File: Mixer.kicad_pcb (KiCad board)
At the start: 2 copper layers, 60 x 100 mm, 44 parts, among them J1 Audio-Jack-2_Switch, J2 Conn_02x05_Odd_Even, J3 Audio-Jack-2_Switch, J4 Audio-Jack-2_Switch, J5 Audio-Jack-2_Switch, J6 Audio-Jack-2_Switch, J7 Audio-Jack-2_Switch, U1 TL074

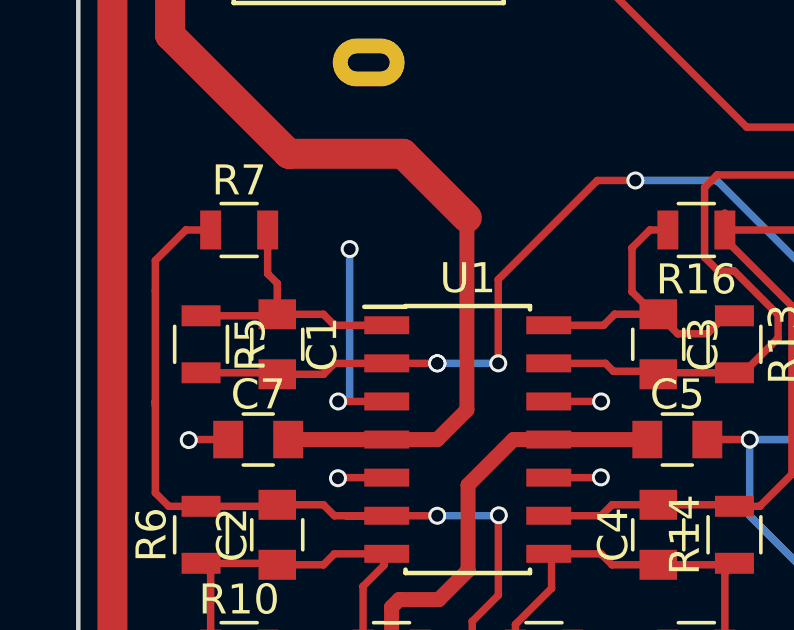
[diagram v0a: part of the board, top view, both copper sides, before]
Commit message: Fixed DRC violation.
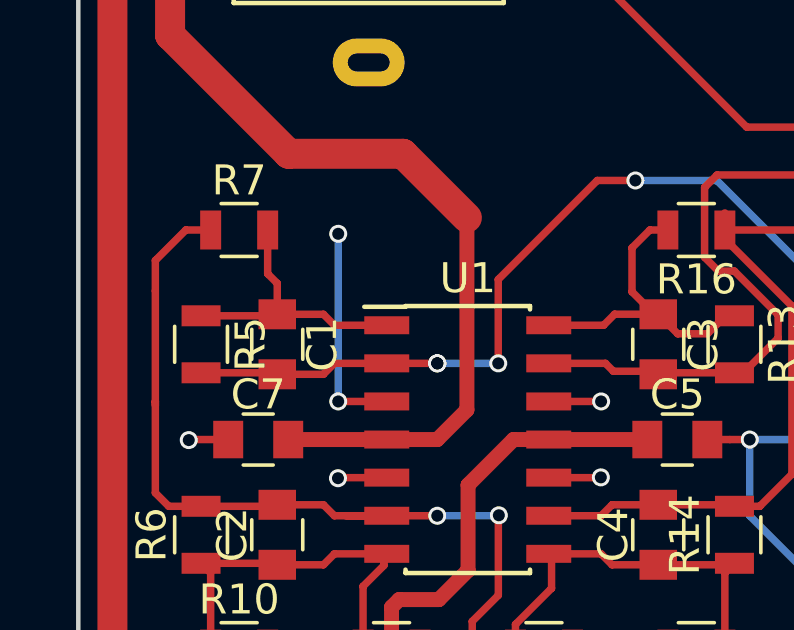
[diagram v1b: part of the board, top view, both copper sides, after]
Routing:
- net GND: track 176.2 -> 176.7 mm
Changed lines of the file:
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@@
   (segment (start 70.485 58.42) (end 70.485 61.065) (width 1) (layer F.Cu) (net 9))
   (segment (start 69.215 57.15) (end 70.485 58.42) (width 1) (layer F.Cu) (net 9))
-  (segment (start 75.565 132.08) (end 75.565 127) (width 0.25) (layer B.Cu) (net 10))
-  (via (at 75.565 127) (size 0.6) (drill 0.4) (layers F.Cu B.Cu) (net 10))
+  (segment (start 75.184 132.08) (end 75.184 126.492) (width 0.25) (layer B.Cu) (net 10))
+  (via (at 75.184 126.492) (size 0.6) (drill 0.4) (layers F.Cu B.Cu) (net 10))
   (segment (start 88.9 133.35) (end 88.9 135.89) (width 0.25) (layer B.Cu) (net 10))
   (via (at 90.805 137.795) (size 0.6) (drill 0.4) (layers F.Cu B.Cu) (net 10))

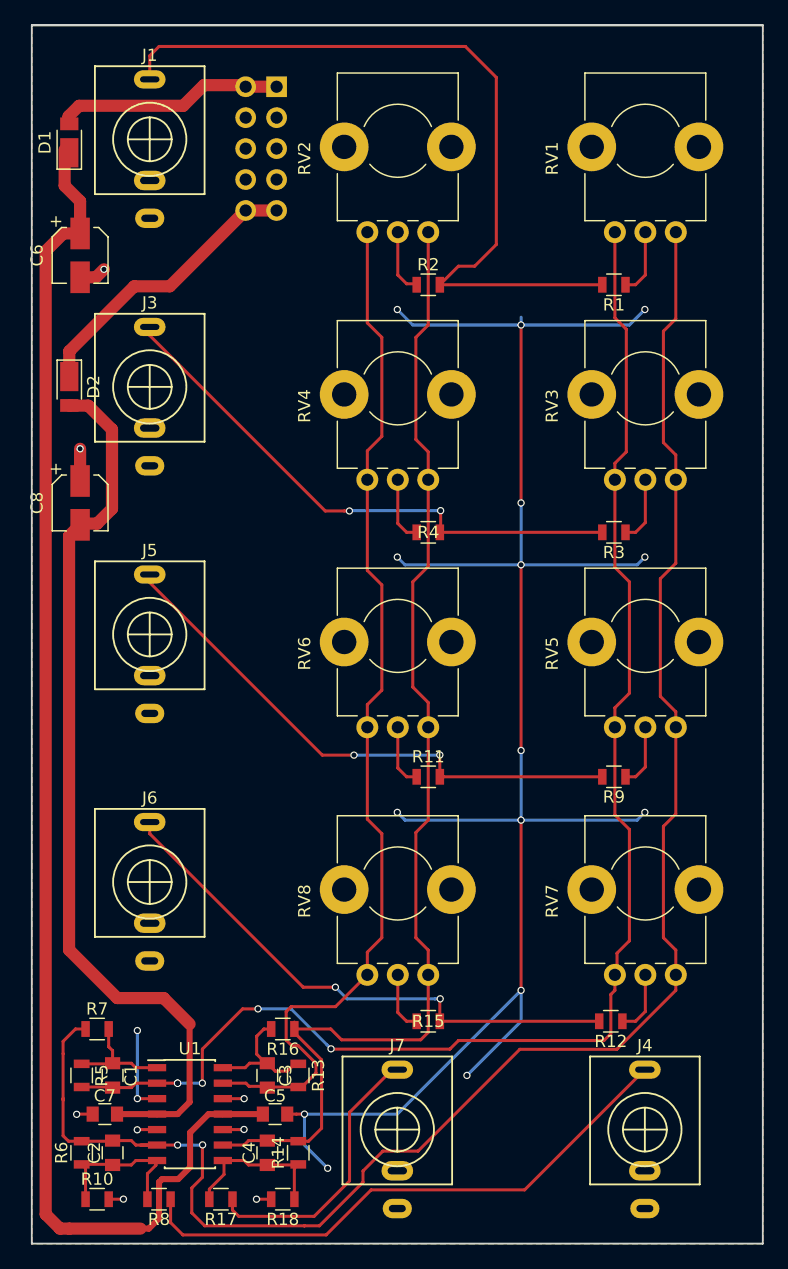
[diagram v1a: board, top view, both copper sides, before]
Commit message: Added configuration resistors.
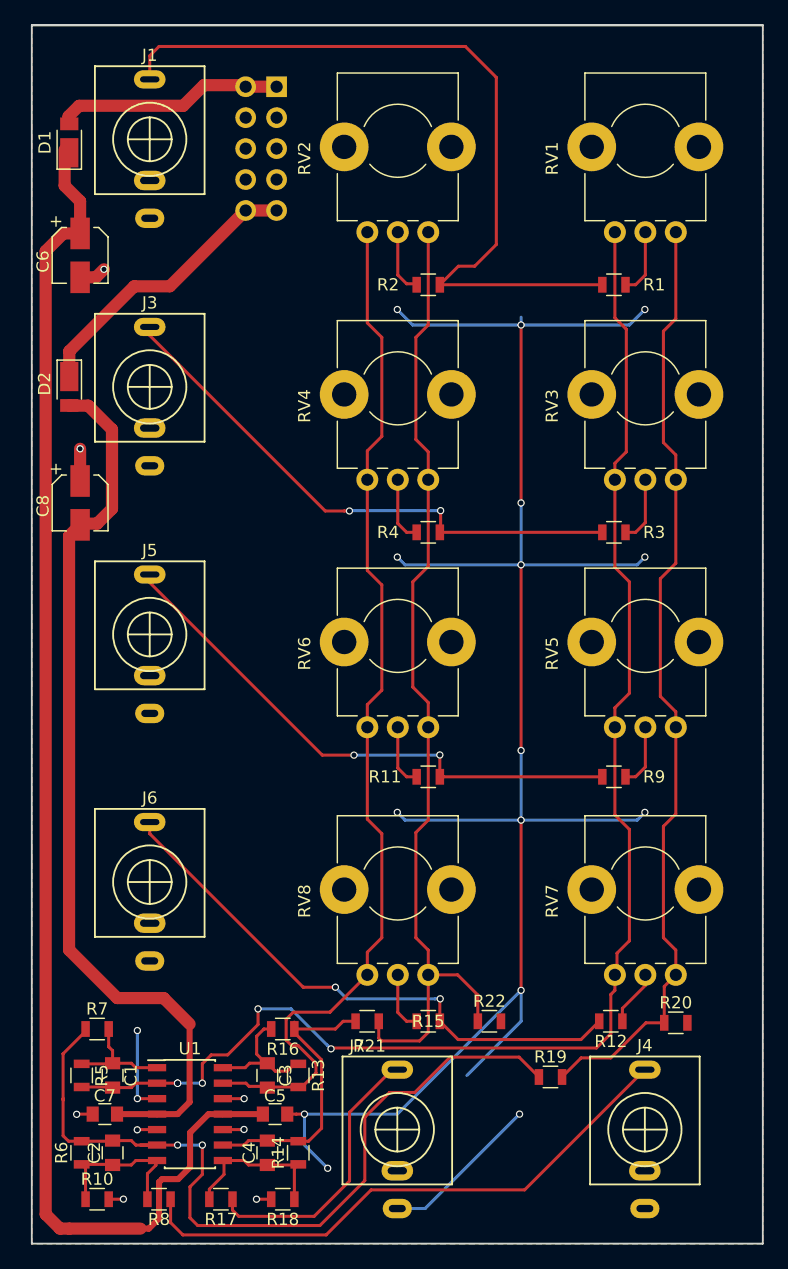
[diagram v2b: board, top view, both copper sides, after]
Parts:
- added R19: 0, Resistors_SMD:R_0805, F.Cu at (109.1, 130.3)
- added R20: 1G, Resistors_SMD:R_0805, F.Cu at (119.4, 125.9)
- added R21: 0, Resistors_SMD:R_0805, F.Cu at (94.0, 125.7)
- added R22: 1G, Resistors_SMD:R_0805, F.Cu at (104.1, 125.7)
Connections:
- RV1 pad 1: Net-(C2-Pad2) -> Net-(R19-Pad2)
- RV2 pad 1: Net-(C4-Pad2) -> Net-(R21-Pad2)
- RV3 pad 1: Net-(C2-Pad2) -> Net-(R19-Pad2)
- RV4 pad 1: Net-(C4-Pad2) -> Net-(R21-Pad2)
- RV5 pad 1: Net-(C2-Pad2) -> Net-(R19-Pad2)
- RV6 pad 1: Net-(C4-Pad2) -> Net-(R21-Pad2)
- RV7 pad 1: Net-(C2-Pad2) -> Net-(R19-Pad2)
- RV8 pad 1: Net-(C4-Pad2) -> Net-(R21-Pad2)
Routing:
- net Net-(R21-Pad2): track 0.00 -> 81.2 mm
- net Net-(R19-Pad2): track 0.00 -> 78.3 mm
- net Net-(C2-Pad2): track 143.2 -> 67.7 mm
- net Net-(C4-Pad2): track 98.4 -> 23.6 mm
- net GND: track 176.7 -> 190.0 mm
- net Net-(J6-Pad1): track 45.4 -> 46.7 mm
- net Net-(R12-Pad1): track 5.22 -> 4.59 mm

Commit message: Silkscreen, edge-cuts and branding.
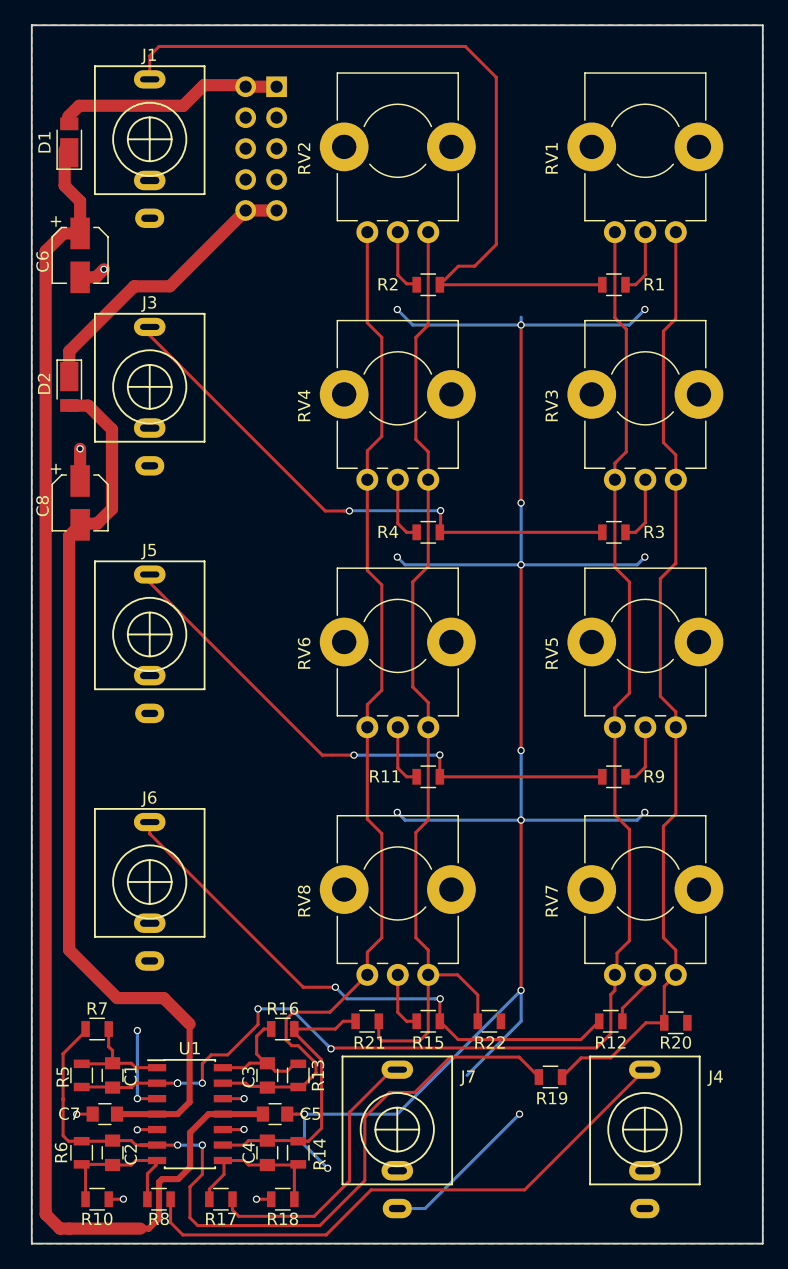
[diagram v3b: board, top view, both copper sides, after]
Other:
- board text added: "+12"
- board text added: "-12"
- board text added: "Modular Mixer, Rev A"
- board text added: "© Marangisto 2018"
